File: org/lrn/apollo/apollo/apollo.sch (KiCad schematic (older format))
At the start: 36 parts, among them Q1 PN2222A, Q2 PN2222A, Q3 PN2222A, Q4 PN2222A, U1 74HC595, U2 5461AS-1, U3 74HC595, U4 ATmega168P-20PU

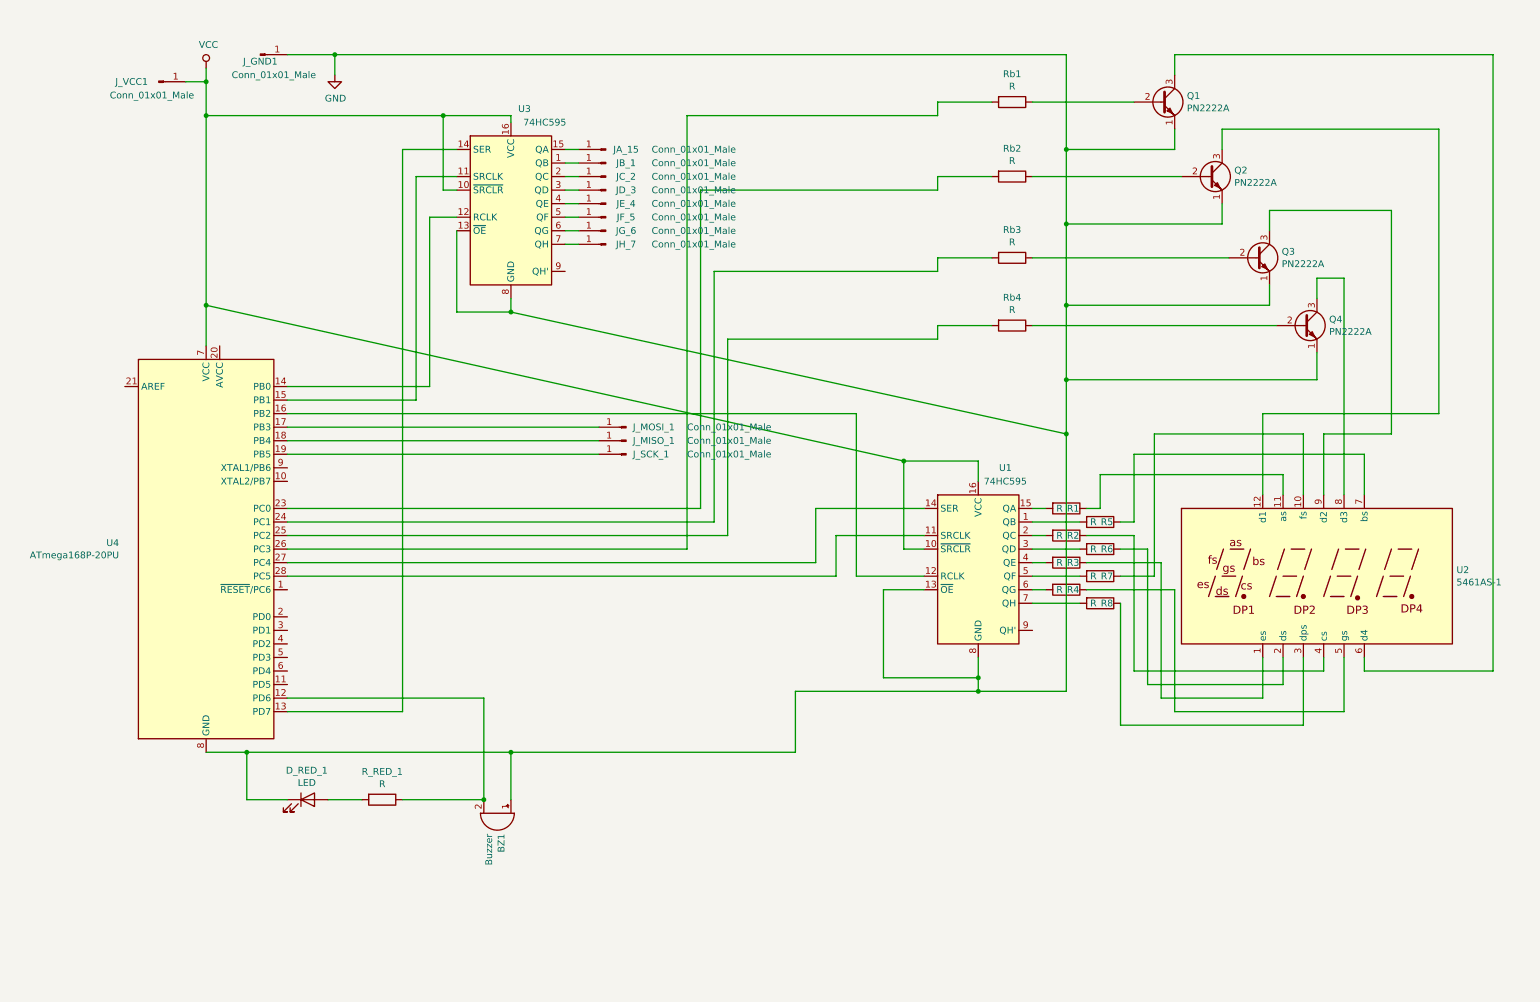
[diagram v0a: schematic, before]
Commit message: apollo: add relay_1 acivate in pin #11
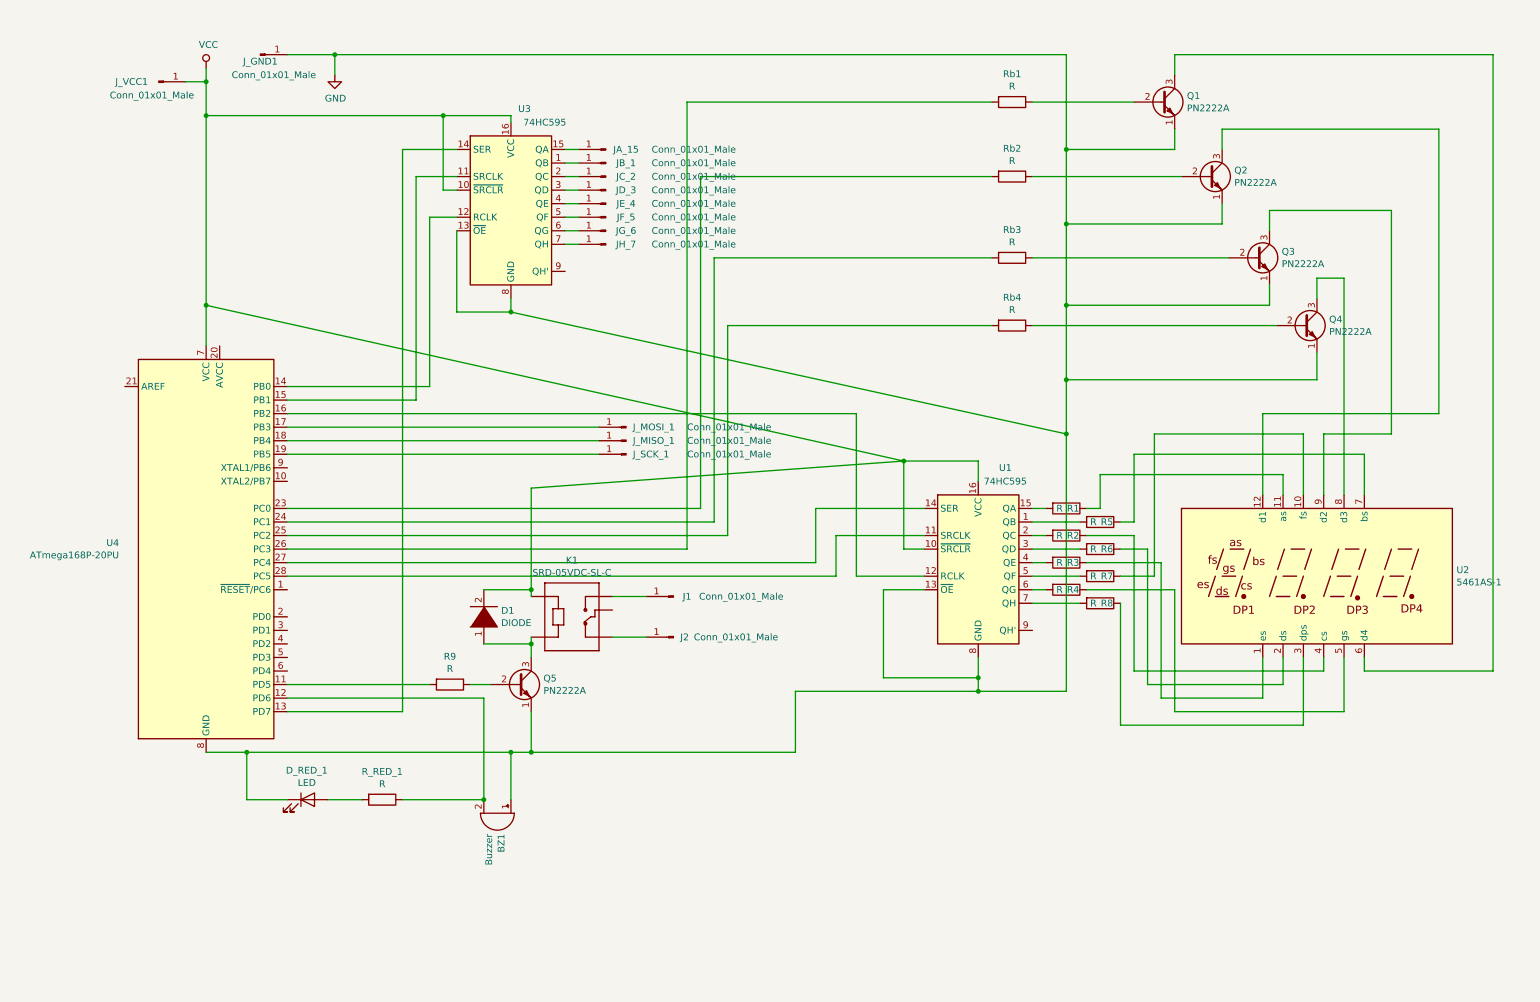
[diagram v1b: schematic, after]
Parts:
- added D1: DIODE, apollo:R__Horizontal, symbol pspice:DIODE
- added J1, J2: Conn_01x01_Male, Connector_Pin:Pin_D0.7mm_L6.5mm_W1.8mm_FlatFork, symbol Connector:Conn_01x01_Male
- added K1: SRD-05VDC-SL-C, apollo:RELAY_SRD-05VDC-SL-C, symbol SRD-05VDC-SL-C:SRD-05VDC-SL-C
- added Q5: PN2222A, apollo:2N222A-TO-92_Wide, symbol Transistor_BJT:PN2222A
- added R9: R, apollo:R__Horizontal, symbol Device:R
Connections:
- net GND: now also Q5.1 (E)
- net VCC: now also D1.2 (A), K1.A1
- net at U4.11 (PD5): now also R9.2
- new net: Q5.2 (B), R9.1
- new net: D1.1 (K), K1.A2, Q5.3 (C)
- new net: J2.1 (Pin_1), K1.NC
- new net: J1.1 (Pin_1), K1.NO
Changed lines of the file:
@@
 Wire Wire Line
 	7050 5400 7050 5250
-Wire Wire Line
-	6750 1800 6750 1700
-Wire Wire Line
-	6750 1700 7150 1700
-Wire Wire Line
-	6750 2400 6750 2300
-Wire Wire Line
-	6750 2300 7150 2300
-Wire Wire Line
-	6750 2800 6750 2900
-Wire Wire Line
-	6750 2900 5200 2900
-Wire Wire Line
-	6750 2800 7150 2800
-Wire Wire Line
-	6750 1250 6750 1150
-Wire Wire Line
-	6750 1150 7150 1150
 $Comp
 L Connector:Conn_01x01_Male J_SCK_1
@@
 $EndComp
 Wire Wire Line
-	5100 4250 5100 2400
-Wire Wire Line
-	5100 2400 6750 2400
-Wire Wire Line
-	5000 4150 5000 1800
-Wire Wire Line
-	5000 1800 6750 1800
-Wire Wire Line
-	4900 1250 4900 4450
-Wire Wire Line
-	4900 1250 6750 1250
-Wire Wire Line
-	5200 2900 5200 4350
+	5100 4250 5100 2300
+Wire Wire Line
+	5000 4150 5000 1700
+Wire Wire Line
+	4900 1150 4900 4450
+Wire Wire Line
+	5200 2800 5200 4350
 Wire Wire Line
 	6150 4650 6650 4650
@@
 Connection ~ 3600 5950
 Wire Wire Line
-	3600 5950 5700 5950
+	3600 5950 3750 5950
+Wire Wire Line
+	5200 2800 7150 2800
+Wire Wire Line
+	5100 2300 7150 2300
+Wire Wire Line
+	5000 1700 7150 1700
+Wire Wire Line
+	4900 1150 7150 1150
+$Comp
+L Device:R R9
+U 1 1 5F75A077
+P 3150 5450
+F 0 "R9" V 2943 5450 50  0000 C CNN
+F 1 "R" V 3034 5450 50  0000 C CNN
+F 2 "apollo:R__Horizontal" V 3080 5450 50  0001 C CNN
+F 3 "~" H 3150 5450 50  0001 C CNN
+	1    3150 5450
+	0    1    1    0
+$EndComp
+$Comp
+L Transistor_BJT:PN2222A Q5
+U 1 1 5F761AF8
+P 3650 5450
+F 0 "Q5" H 3840 5496 50  0000 L CNN
+F 1 "PN2222A" H 3840 5405 50  0000 L CNN
+F 2 "apollo:2N222A-TO-92_Wide" H 3850 5375 50  0001 L CIN
+F 3 "http://www.fairchildsemi.com/ds/PN/PN2222A.pdf" H 3650 5450 50  0001 L CNN
+	1    3650 5450
+	1    0    0    -1
+$EndComp
+Wire Wire Line
+	1950 5450 3000 5450
+Wire Wire Line
+	3300 5450 3450 5450
+$Comp
+L SRD-05VDC-SL-C:SRD-05VDC-SL-C K1
+U 1 1 5F789B70
+P 4050 4900
+F 0 "K1" H 4050 5267 50  0000 C CNN
+F 1 "SRD-05VDC-SL-C" H 4050 5176 50  0000 C CNN
+F 2 "apollo:RELAY_SRD-05VDC-SL-C" H 4050 4900 50  0001 L BNN
+F 3 "IPC-7251" H 4050 4900 50  0001 L BNN
+F 4 "SONGLE RELAY" H 4050 4900 50  0001 L BNN "Field4"
+	1    4050 4900
+	1    0    0    -1
+$EndComp
+Wire Wire Line
+	3750 5250 3750 5150
+Wire Wire Line
+	6500 3800 3750 4000
+Wire Wire Line
+	3750 4000 3750 4750
+$Comp
+L pspice:DIODE D1
+U 1 1 5F7DF449
+P 3400 4950
+F 0 "D1" V 3446 4822 50  0000 R CNN
+F 1 "DIODE" V 3355 4822 50  0000 R CNN
+F 2 "apollo:R__Horizontal" H 3400 4950 50  0001 C CNN
+F 3 "~" H 3400 4950 50  0001 C CNN
+	1    3400 4950
+	0    -1   -1   0
+$EndComp
+Wire Wire Line
+	3400 4750 3750 4750
+Connection ~ 3750 4750
+Wire Wire Line
+	3750 4750 3750 4800
+Wire Wire Line
+	3400 5150 3750 5150
+Connection ~ 3750 5150
+Wire Wire Line
+	3750 5150 3750 5100
+$Comp
+L Connector:Conn_01x01_Male J2
+U 1 1 5F7F3157
+P 4800 5100
+F 0 "J2" H 4750 5100 50  0000 R CNN
+F 1 "Conn_01x01_Male" H 4650 5100 50  0000 R CNN
+F 2 "Connector_Pin:Pin_D0.7mm_L6.5mm_W1.8mm_FlatFork" H 4800 5100 50  0001 C CNN
+F 3 "~" H 4800 5100 50  0001 C CNN
+	1    4800 5100
+	-1   0    0    1
+$EndComp
+$Comp
+L Connector:Conn_01x01_Male J1
+U 1 1 5F7F3A36
+P 4800 4800
+F 0 "J1" H 4700 4800 50  0000 C CNN
+F 1 "Conn_01x01_Male" H 4300 4800 50  0000 C CNN
+F 2 "Connector_Pin:Pin_D0.7mm_L6.5mm_W1.8mm_FlatFork" H 4800 4800 50  0001 C CNN
+F 3 "~" H 4800 4800 50  0001 C CNN
+	1    4800 4800
+	-1   0    0    1
+$EndComp
+Wire Wire Line
+	4350 5100 4600 5100
+Wire Wire Line
+	4350 4800 4600 4800
+Wire Wire Line
+	3750 5650 3750 5950
+Connection ~ 3750 5950
+Wire Wire Line
+	3750 5950 5700 5950
 $EndSCHEMATC

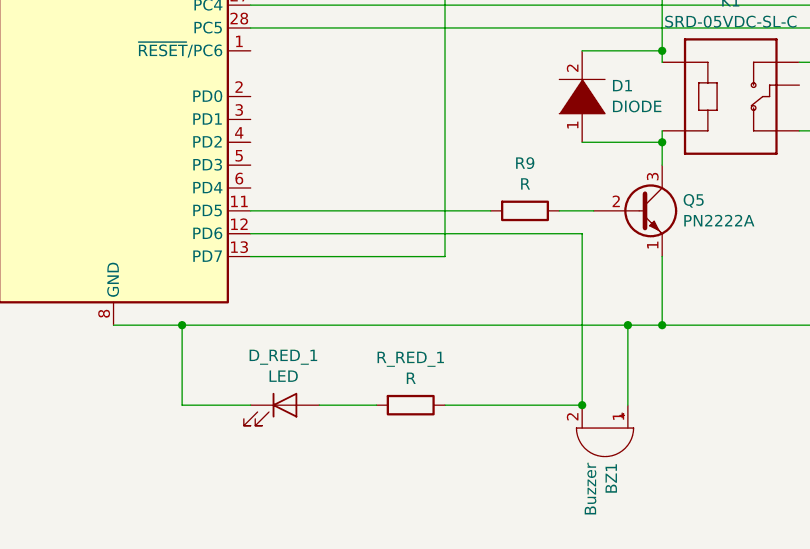
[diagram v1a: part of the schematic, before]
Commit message: apollo: update schematic and pcb for relay_1
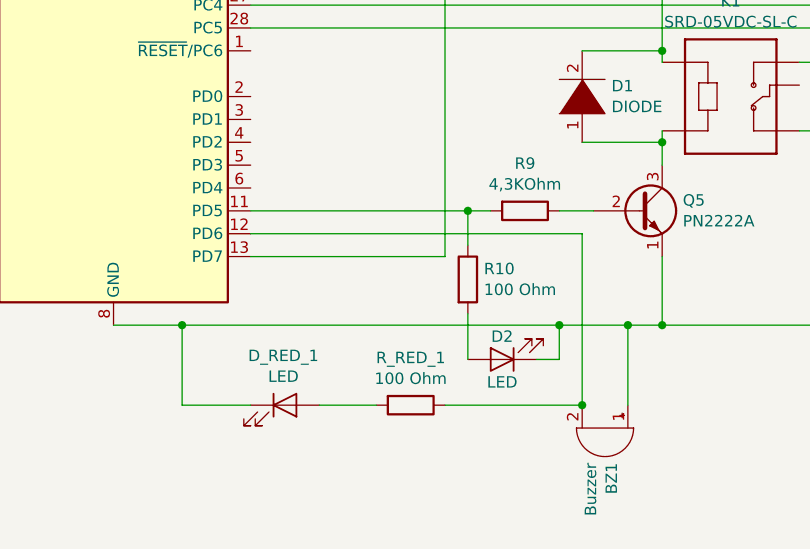
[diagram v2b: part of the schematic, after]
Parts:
- added D2: LED, LED_THT:LED_D5.0mm_FlatTop, symbol Device:LED
- added R10: 100 Ohm, apollo:R__Horizontal, symbol Device:R
- R9: value R -> 4,3KOhm
- R_RED_1: value R -> 100 Ohm
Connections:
- net GND: now also D2.1 (K)
- net at R9.2, U4.11 (PD5): now also R10.1
- new net: D2.2 (A), R10.2
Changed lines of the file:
@@
 Connection ~ 1650 5950
 Wire Wire Line
-	1650 5950 3600 5950
+	1650 5950 3300 5950
 $Comp
 L Device:R R_RED_1
@@
 P 2650 6300
 F 0 "R_RED_1" V 2443 6300 50  0000 C CNN
-F 1 "R" V 2534 6300 50  0000 C CNN
+F 1 "100 Ohm" V 2534 6300 50  0000 C CNN
 F 2 "apollo:R__Horizontal" V 2580 6300 50  0001 C CNN
 F 3 "~" H 2650 6300 50  0001 C CNN
@@
 P 3150 5450
 F 0 "R9" V 2943 5450 50  0000 C CNN
-F 1 "R" V 3034 5450 50  0000 C CNN
+F 1 "4,3KOhm" V 3034 5450 50  0000 C CNN
 F 2 "apollo:R__Horizontal" V 3080 5450 50  0001 C CNN
 F 3 "~" H 3150 5450 50  0001 C CNN
@@
 $EndComp
 Wire Wire Line
-	1950 5450 3000 5450
+	1950 5450 2900 5450
 Wire Wire Line
 	3300 5450 3450 5450
@@
 Wire Wire Line
 	3750 5950 5700 5950
+$Comp
+L Device:R R10
+U 1 1 5F73C2C8
+P 2900 5750
+F 0 "R10" H 2970 5796 50  0000 L CNN
+F 1 "100 Ohm" H 2970 5705 50  0000 L CNN
+F 2 "apollo:R__Horizontal" V 2830 5750 50  0001 C CNN
+F 3 "~" H 2900 5750 50  0001 C CNN
+	1    2900 5750
+	1    0    0    -1
+$EndComp
+Wire Wire Line
+	2900 5450 2900 5600
+Connection ~ 2900 5450
+Wire Wire Line
+	2900 5450 3000 5450
+$Comp
+L Device:LED D2
+U 1 1 5F7461AA
+P 3050 6100
+F 0 "D2" H 3050 6000 50  0000 C CNN
+F 1 "LED" H 3050 6200 50  0000 C CNN
+F 2 "LED_THT:LED_D5.0mm_FlatTop" H 3050 6100 50  0001 C CNN
+F 3 "~" H 3050 6100 50  0001 C CNN
+	1    3050 6100
+	-1   0    0    1
+$EndComp
+Wire Wire Line
+	2900 5900 2900 6100
+Wire Wire Line
+	3200 6100 3300 6100
+Wire Wire Line
+	3300 6100 3300 5950
+Connection ~ 3300 5950
+Wire Wire Line
+	3300 5950 3600 5950
 $EndSCHEMATC

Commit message: apollo: pcb updated
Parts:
- added J10, J11, J3, J4, J5, J6, J7, J8, J9: Conn_01x01_Male, Connector_Pin:Pin_D0.7mm_L6.5mm_W1.8mm_FlatFork, symbol Connector:Conn_01x01_Male
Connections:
- net at U4.1 (~RESET~/PC6): now also J6.1 (Pin_1)
- net at U4.10 (XTAL2/PB7): now also J5.1 (Pin_1)
- net at U4.2 (PD0): now also J7.1 (Pin_1)
- net at U4.3 (PD1): now also J8.1 (Pin_1)
- net at U4.4 (PD2): now also J9.1 (Pin_1)
- net at U4.5 (PD3): now also J10.1 (Pin_1)
- net at U4.6 (PD4): now also J11.1 (Pin_1)
- net at U4.9 (XTAL1/PB6): now also J4.1 (Pin_1)
- net at K1.COM: now also J3.1 (Pin_1)
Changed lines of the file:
@@
 Wire Wire Line
 	3300 5950 3600 5950
+$Comp
+L Connector:Conn_01x01_Male J3
+U 1 1 5F74C3F1
+P 4800 4950
+F 0 "J3" H 4700 4950 50  0000 C CNN
+F 1 "Conn_01x01_Male" H 4300 4950 50  0000 C CNN
+F 2 "Connector_Pin:Pin_D0.7mm_L6.5mm_W1.8mm_FlatFork" H 4800 4950 50  0001 C CNN
+F 3 "~" H 4800 4950 50  0001 C CNN
+	1    4800 4950
+	-1   0    0    1
+$EndComp
+Wire Wire Line
+	4350 4900 4600 4900
+Wire Wire Line
+	4600 4900 4600 4950
+$Comp
+L Connector:Conn_01x01_Male J4
+U 1 1 5F784BB5
+P 2250 3850
+F 0 "J4" H 2150 3850 50  0000 C CNN
+F 1 "Conn_01x01_Male" H 1750 3850 50  0000 C CNN
+F 2 "Connector_Pin:Pin_D0.7mm_L6.5mm_W1.8mm_FlatFork" H 2250 3850 50  0001 C CNN
+F 3 "~" H 2250 3850 50  0001 C CNN
+	1    2250 3850
+	-1   0    0    1
+$EndComp
+$Comp
+L Connector:Conn_01x01_Male J5
+U 1 1 5F78ED5D
+P 2250 3950
+F 0 "J5" H 2150 3950 50  0000 C CNN
+F 1 "Conn_01x01_Male" H 1750 3950 50  0000 C CNN
+F 2 "Connector_Pin:Pin_D0.7mm_L6.5mm_W1.8mm_FlatFork" H 2250 3950 50  0001 C CNN
+F 3 "~" H 2250 3950 50  0001 C CNN
+	1    2250 3950
+	-1   0    0    1
+$EndComp
+Wire Wire Line
+	1950 3850 2050 3850
+Wire Wire Line
+	1950 3950 2050 3950
+$Comp
+L Connector:Conn_01x01_Male J6
+U 1 1 5F7B08FE
+P 2250 4750
+F 0 "J6" H 2150 4750 50  0000 C CNN
+F 1 "Conn_01x01_Male" H 1750 4750 50  0000 C CNN
+F 2 "Connector_Pin:Pin_D0.7mm_L6.5mm_W1.8mm_FlatFork" H 2250 4750 50  0001 C CNN
+F 3 "~" H 2250 4750 50  0001 C CNN
+	1    2250 4750
+	-1   0    0    1
+$EndComp
+Wire Wire Line
+	1950 4750 2050 4750
+$Comp
+L Connector:Conn_01x01_Male J7
+U 1 1 5F7C58F9
+P 2250 4950
+F 0 "J7" H 2150 4950 50  0000 C CNN
+F 1 "Conn_01x01_Male" H 1750 4950 50  0000 C CNN
+F 2 "Connector_Pin:Pin_D0.7mm_L6.5mm_W1.8mm_FlatFork" H 2250 4950 50  0001 C CNN
+F 3 "~" H 2250 4950 50  0001 C CNN
+	1    2250 4950
+	-1   0    0    1
+$EndComp
+$Comp
+L Connector:Conn_01x01_Male J8
+U 1 1 5F7D01AC
+P 2250 5050
+F 0 "J8" H 2150 5050 50  0000 C CNN
+F 1 "Conn_01x01_Male" H 1750 5050 50  0000 C CNN
+F 2 "Connector_Pin:Pin_D0.7mm_L6.5mm_W1.8mm_FlatFork" H 2250 5050 50  0001 C CNN
+F 3 "~" H 2250 5050 50  0001 C CNN
+	1    2250 5050
+	-1   0    0    1
+$EndComp
+$Comp
+L Connector:Conn_01x01_Male J9
+U 1 1 5F7DAA9F
+P 2250 5150
+F 0 "J9" H 2150 5150 50  0000 C CNN
+F 1 "Conn_01x01_Male" H 1750 5150 50  0000 C CNN
+F 2 "Connector_Pin:Pin_D0.7mm_L6.5mm_W1.8mm_FlatFork" H 2250 5150 50  0001 C CNN
+F 3 "~" H 2250 5150 50  0001 C CNN
+	1    2250 5150
+	-1   0    0    1
+$EndComp
+$Comp
+L Connector:Conn_01x01_Male J10
+U 1 1 5F7E535B
+P 2250 5250
+F 0 "J10" H 2150 5250 50  0000 C CNN
+F 1 "Conn_01x01_Male" H 1750 5250 50  0000 C CNN
+F 2 "Connector_Pin:Pin_D0.7mm_L6.5mm_W1.8mm_FlatFork" H 2250 5250 50  0001 C CNN
+F 3 "~" H 2250 5250 50  0001 C CNN
+	1    2250 5250
+	-1   0    0    1
+$EndComp
+$Comp
+L Connector:Conn_01x01_Male J11
+U 1 1 5F7EFCF4
+P 2250 5350
+F 0 "J11" H 2150 5350 50  0000 C CNN
+F 1 "Conn_01x01_Male" H 1750 5350 50  0000 C CNN
+F 2 "Connector_Pin:Pin_D0.7mm_L6.5mm_W1.8mm_FlatFork" H 2250 5350 50  0001 C CNN
+F 3 "~" H 2250 5350 50  0001 C CNN
+	1    2250 5350
+	-1   0    0    1
+$EndComp
+Wire Wire Line
+	1950 4950 2050 4950
+Wire Wire Line
+	1950 5050 2050 5050
+Wire Wire Line
+	1950 5150 2050 5150
+Wire Wire Line
+	1950 5250 2050 5250
+Wire Wire Line
+	1950 5350 2050 5350
 $EndSCHEMATC
